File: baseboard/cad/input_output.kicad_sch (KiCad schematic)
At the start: 31 parts, among them J1 DC POWER JACK, J2 1/4" JACK, STEREO, J3 6-440054-2, J4 6-440129-2, J5 1/4" JACK, STEREO, U1 N/A, U2 N/A, U3 N/A, U4 N/A, U5 N/A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

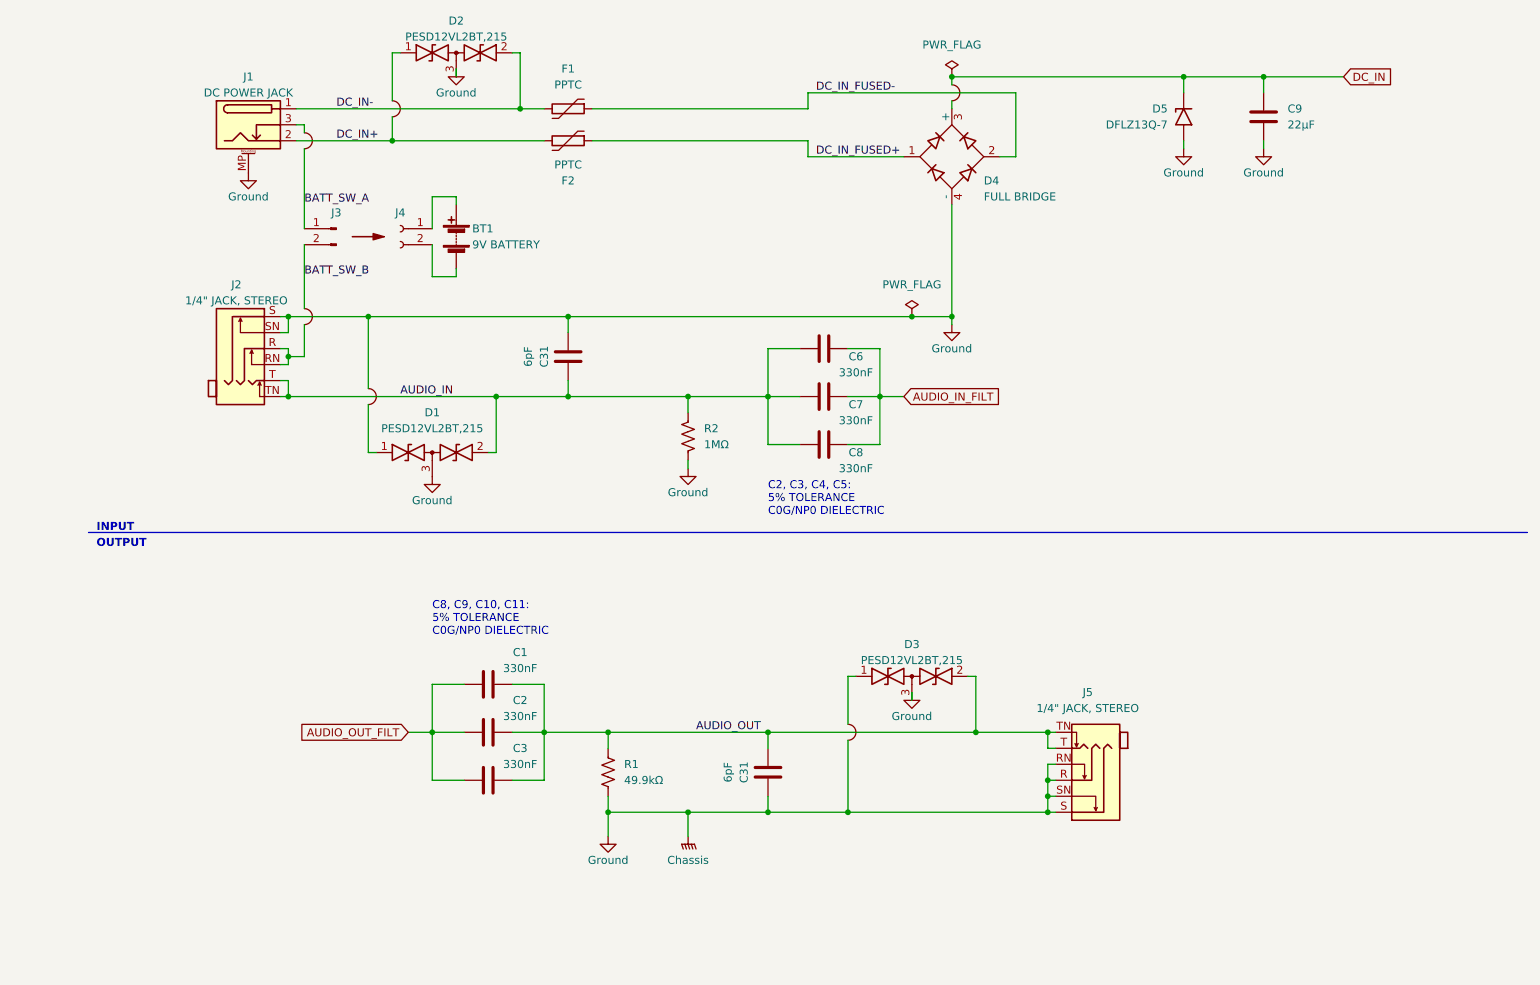
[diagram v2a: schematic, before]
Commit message: swapped micro and started layout
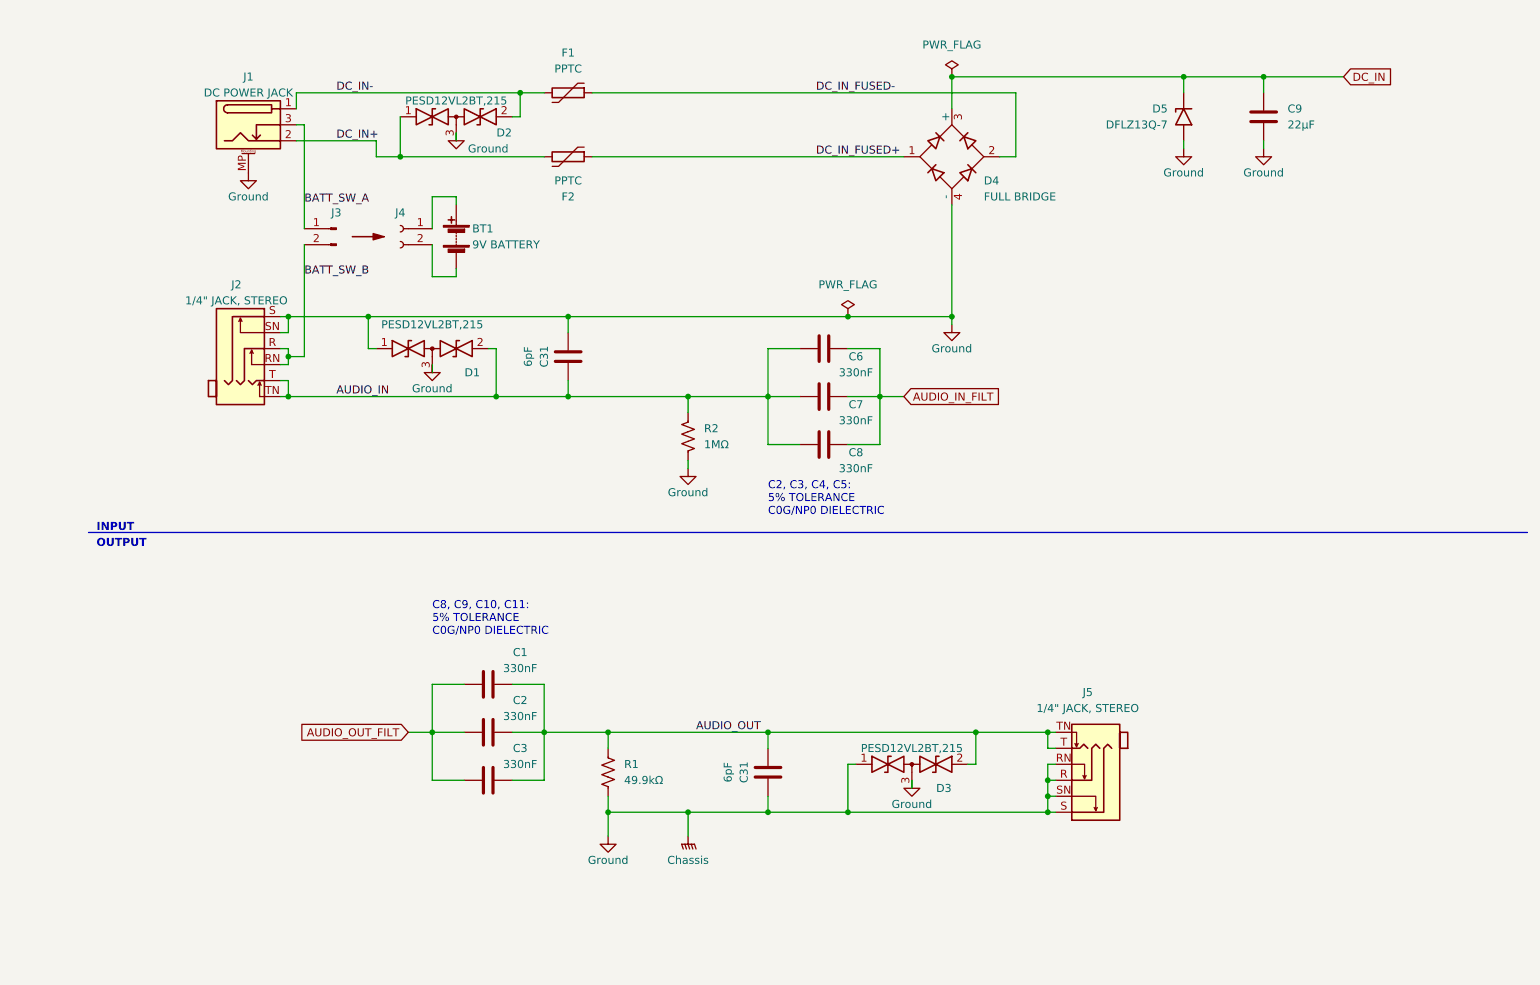
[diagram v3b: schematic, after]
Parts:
- removed U1, U2, U3, U4, U5, U6: N/A, N/A, symbol Library:Symbol_Jumper
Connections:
- net BATT_SW_A: now also J1.3
- net BATT_SW_B: now also J2.R, J2.RN
- net DC_IN: now also D4.3 (+)
- net DC_IN+: now also D2.1 (A1)
- net GND: now also D1.1 (A1), D3.1 (A1)
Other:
- moved on the sheet: D1, D2, D3, F1, F2

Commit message: swapped relays for nice analog switch, saved $4
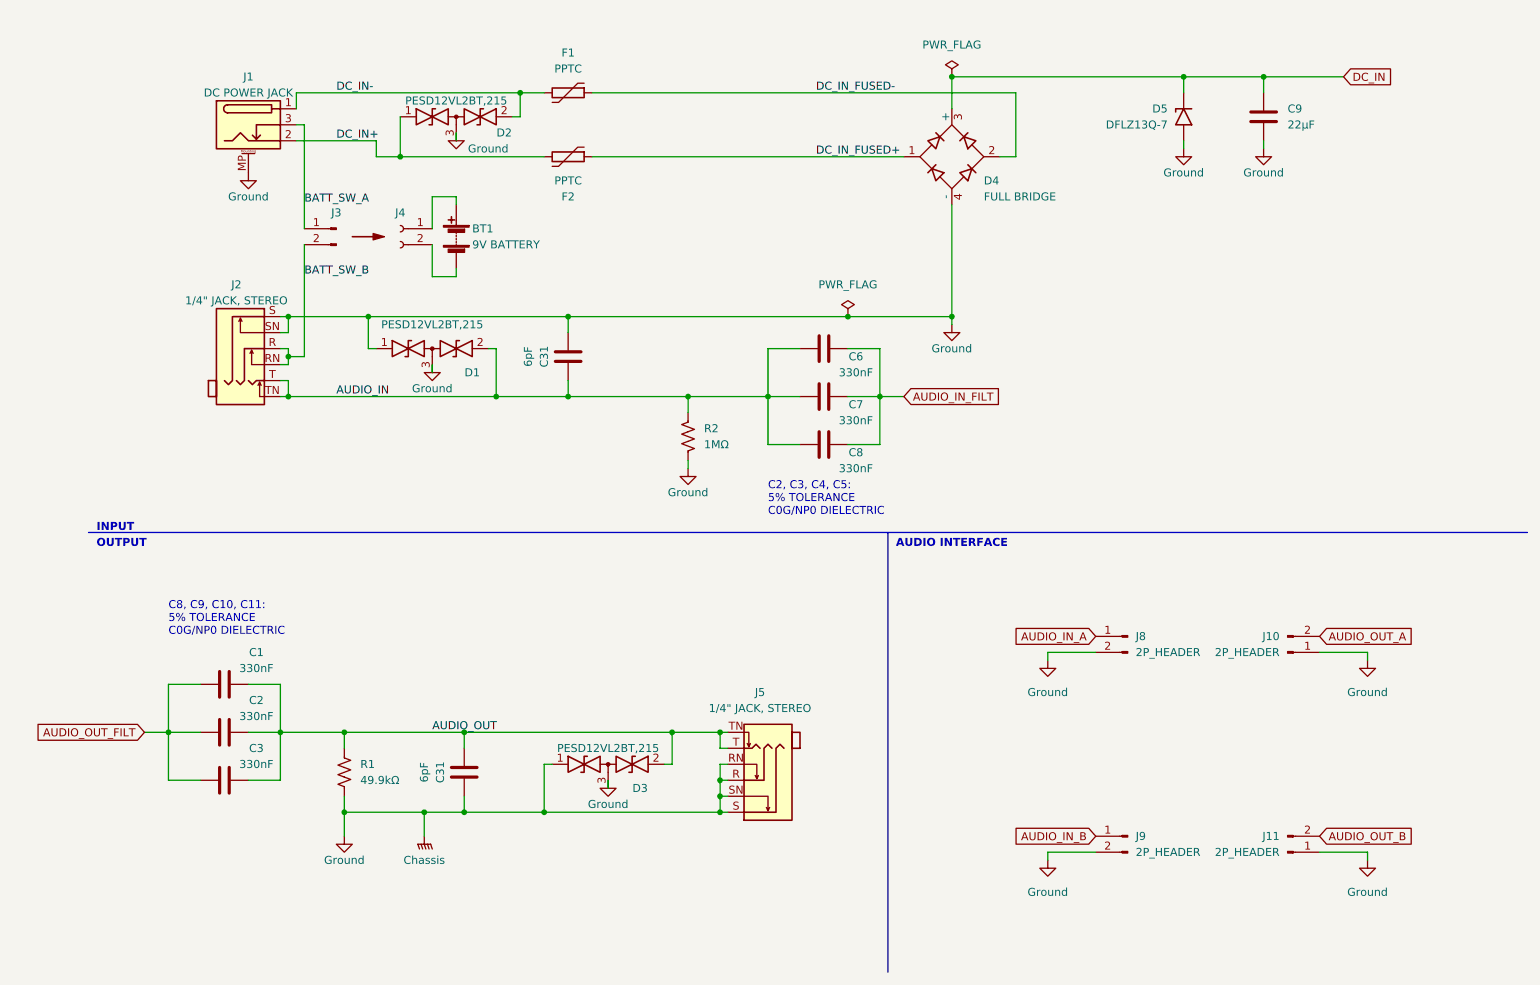
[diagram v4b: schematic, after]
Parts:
- added J10, J11, J8, J9: 2P_HEADER, Connector_PinSocket_2.54mm:PinSocket_1x02_P2.54mm_Vertical, symbol Connector:Conn_01x02_Male
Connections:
- net GND: now also J10.1 (Pin_1), J11.1 (Pin_1), J8.2 (Pin_2), J9.2 (Pin_2)
- new net AUDIO_IN_A: J8.1 (Pin_1)
- new net AUDIO_IN_B: J9.1 (Pin_1)
- new net AUDIO_OUT_A: J10.2 (Pin_2)
- new net AUDIO_OUT_B: J11.2 (Pin_2)
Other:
- note added: "AUDIO INTERFACE"
- moved on the sheet: C1, C2, C3, C31, D3, J5, R1
